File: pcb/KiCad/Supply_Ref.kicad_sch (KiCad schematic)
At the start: 31 parts, among them J2 RF_Shield_One_Piece DNF, J22 GND, U1 LT3032-12, U9 LT8610

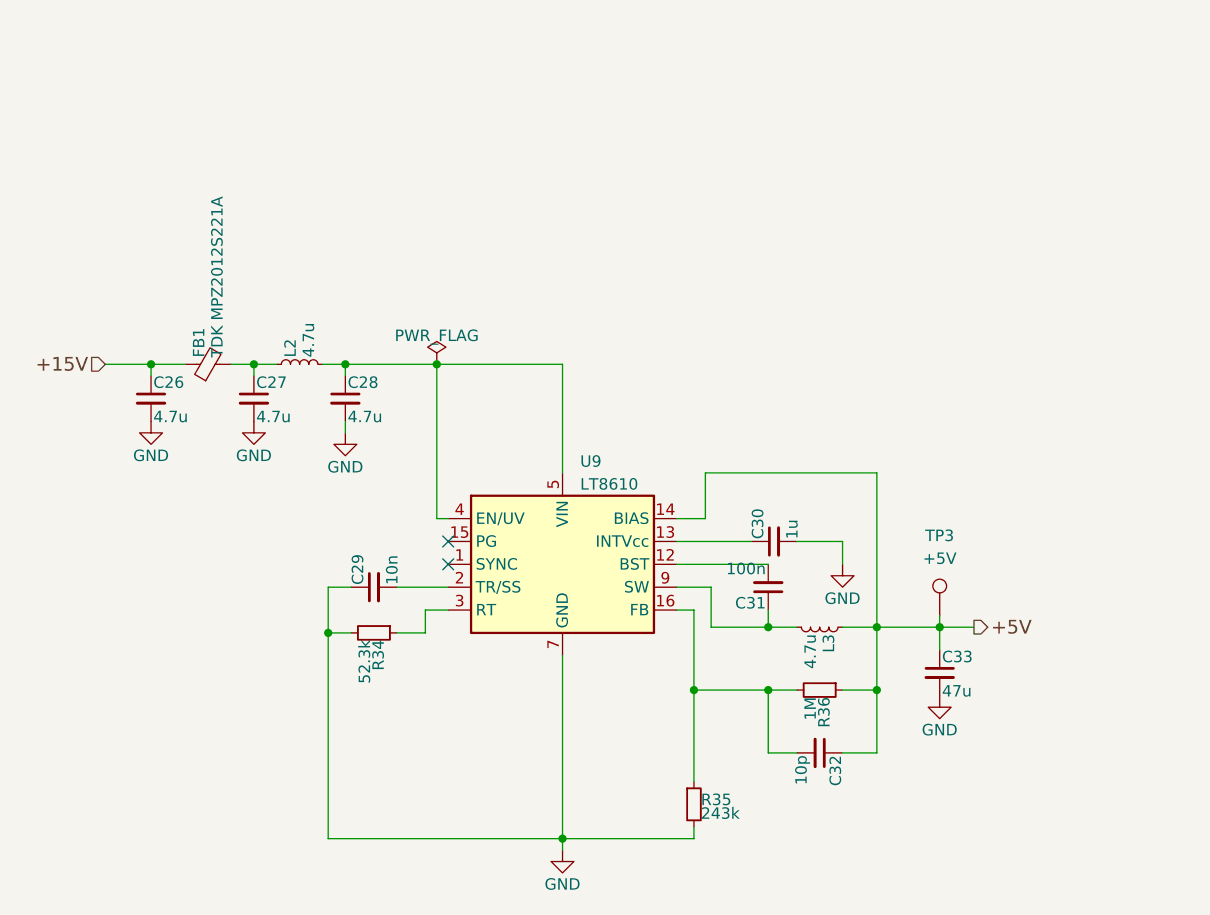
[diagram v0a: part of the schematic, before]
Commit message: Fixed off-grid positioning
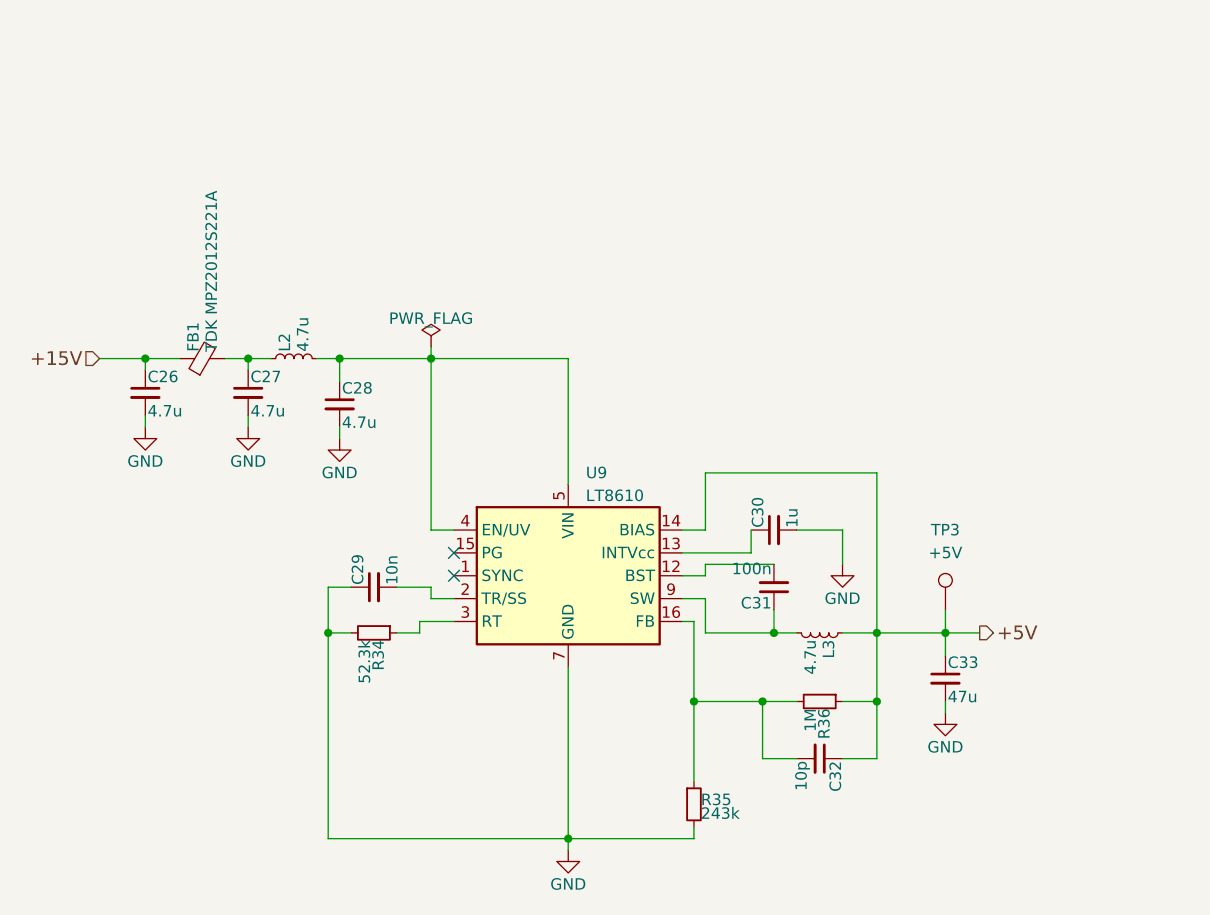
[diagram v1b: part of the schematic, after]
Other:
- moved on the sheet: C26, C27, C28, C30, C31, C32, C33, FB1, L2, L3, R36, TP3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
